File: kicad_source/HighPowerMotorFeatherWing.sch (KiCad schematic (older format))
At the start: 2 parts, among them CN1 ADAFRUIT_FEATHER

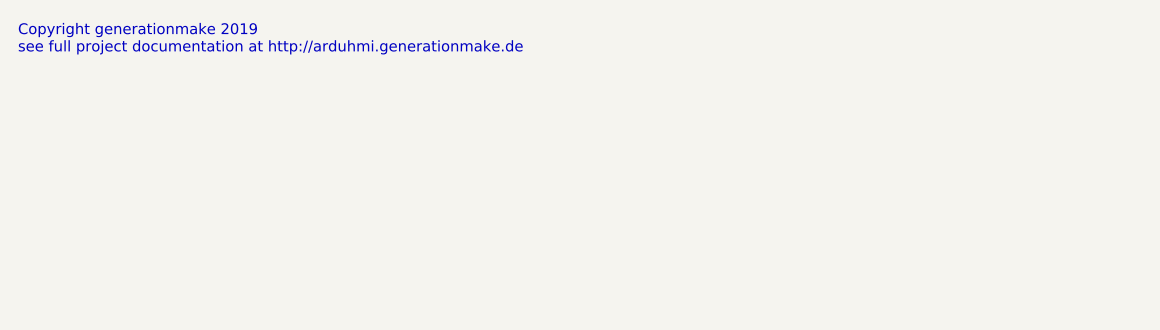
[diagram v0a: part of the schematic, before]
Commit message: added values in schematic, generated pdf schematic
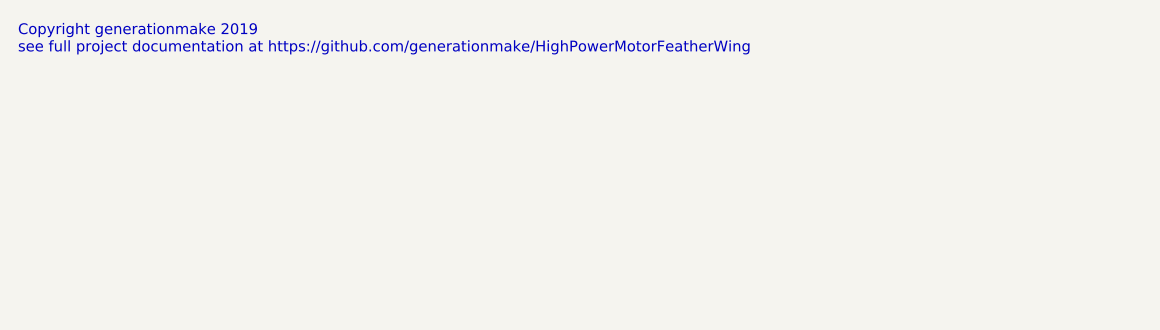
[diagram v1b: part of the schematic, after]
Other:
- note added: "Copyright generationmake 2019\nsee full project documentation at https://github.com/generationmake/HighPowerMotorFeatherWing"
- note removed: "Copyright generationmake 2019\nsee full project documentation at http://arduhmi.generationmake.de"
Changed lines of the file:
@@
 EESchema Schematic File Version 4
-LIBS:HighPowerMotorFeatherWing-cache
-EELAYER 26 0
+EELAYER 30 0
 EELAYER END
 $Descr A4 11693 8268
@@
 Sheet 1 5
 Title "HighPowerMotorFeatherWing"
-Date "2019-12-01"
+Date "2019-12-29"
 Rev "1.0"
 Comp "generationmake"
@@
 $EndDescr
 Text Notes 500  650  0    47   ~ 0
-Copyright generationmake 2019\nsee full project documentation at http://arduhmi.generationmake.de
+Copyright generationmake 2019\nsee full project documentation at https://github.com/generationmake/HighPowerMotorFeatherWing
 Text Notes 7000 6900 0    43   ~ 0
 You may redistribute and modify this documentation under the terms of the CERN OHL v.1.2. (http://ohwr.org/cernohl). \nThis documentation is distributed WITHOUT ANY EXPRESS OR IMPLIED WARRANTY, INCLUDING OF MERCHANTABILITY, SATISFACTORY \nQUALITY AND FITNESS FOR A PARTICULAR PURPOSE. Please see the CERN OHL v.1.2  for applicable conditions
